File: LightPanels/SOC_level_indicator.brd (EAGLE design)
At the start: 161.2 x 162.3 mm, 163 parts, among them IC1 LM1084-ADJ

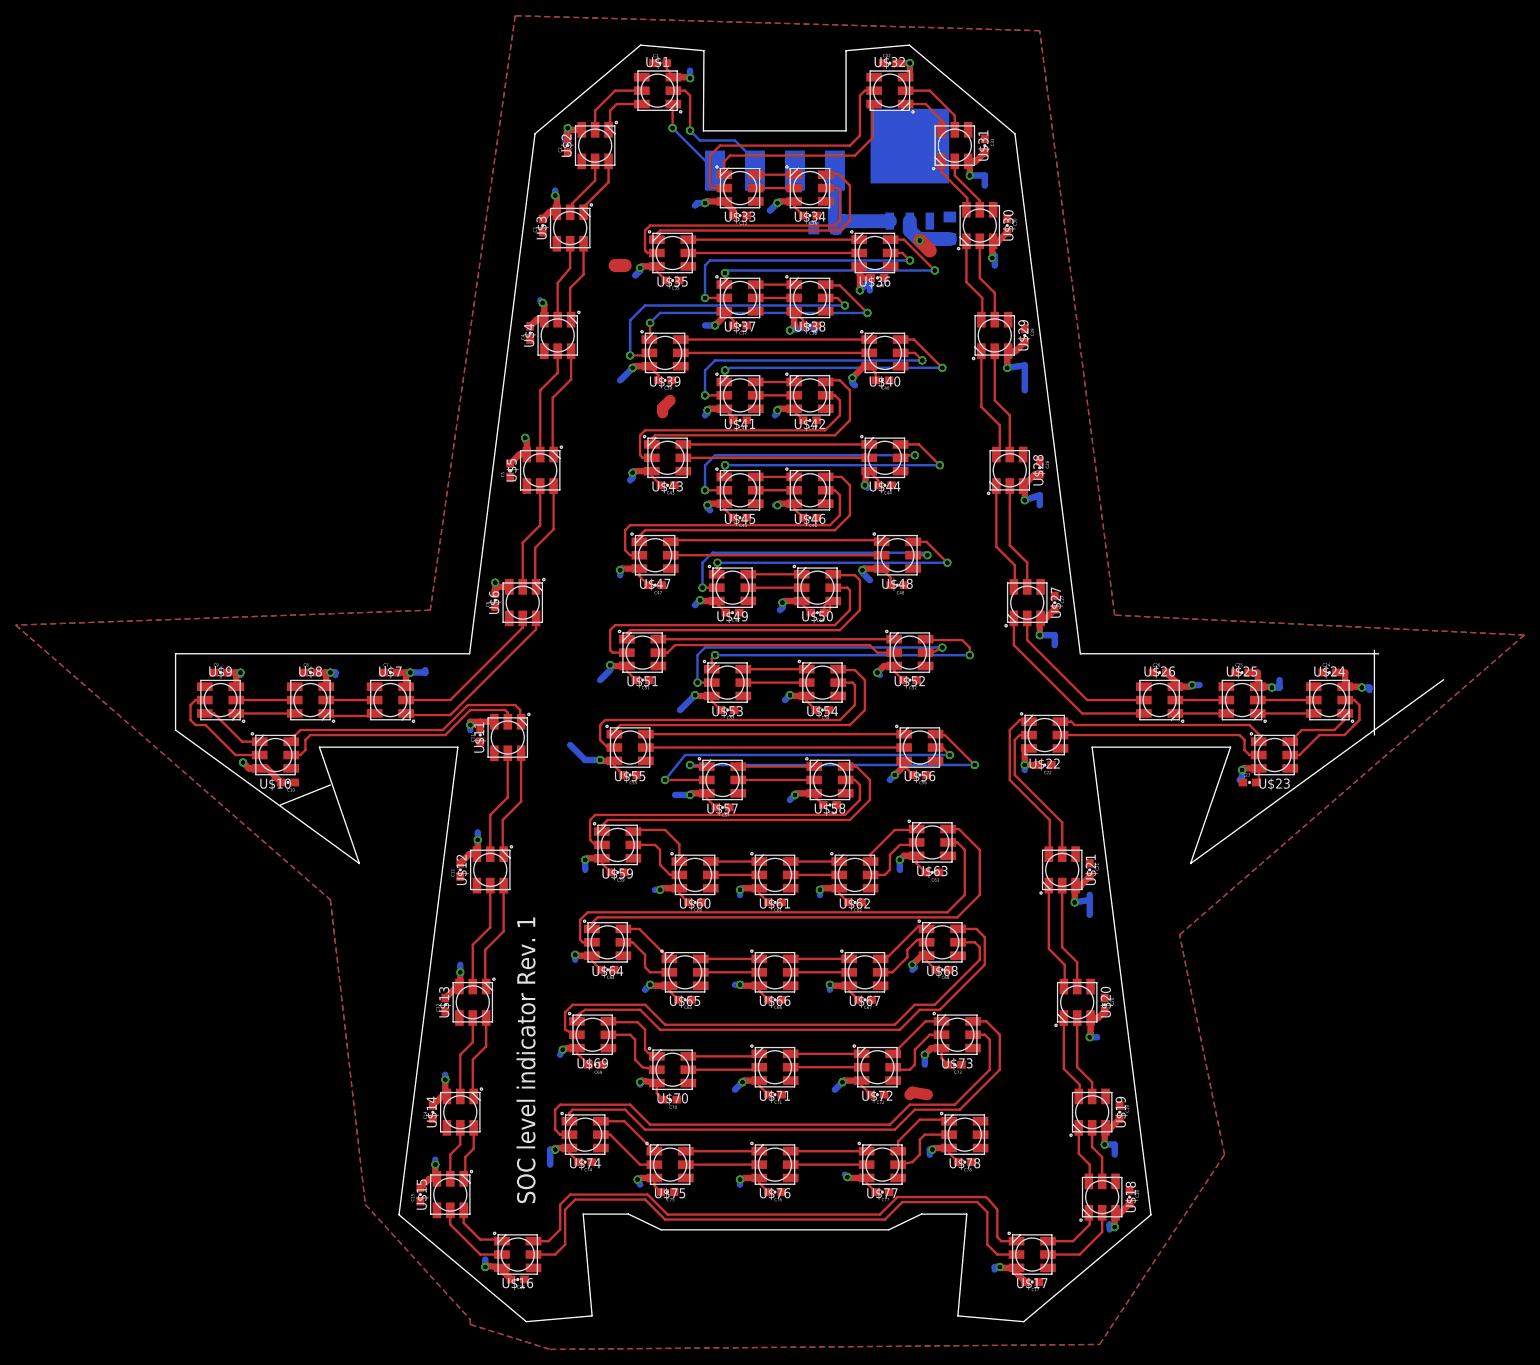
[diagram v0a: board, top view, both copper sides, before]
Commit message: Clean up light panels. Remvoe names/values
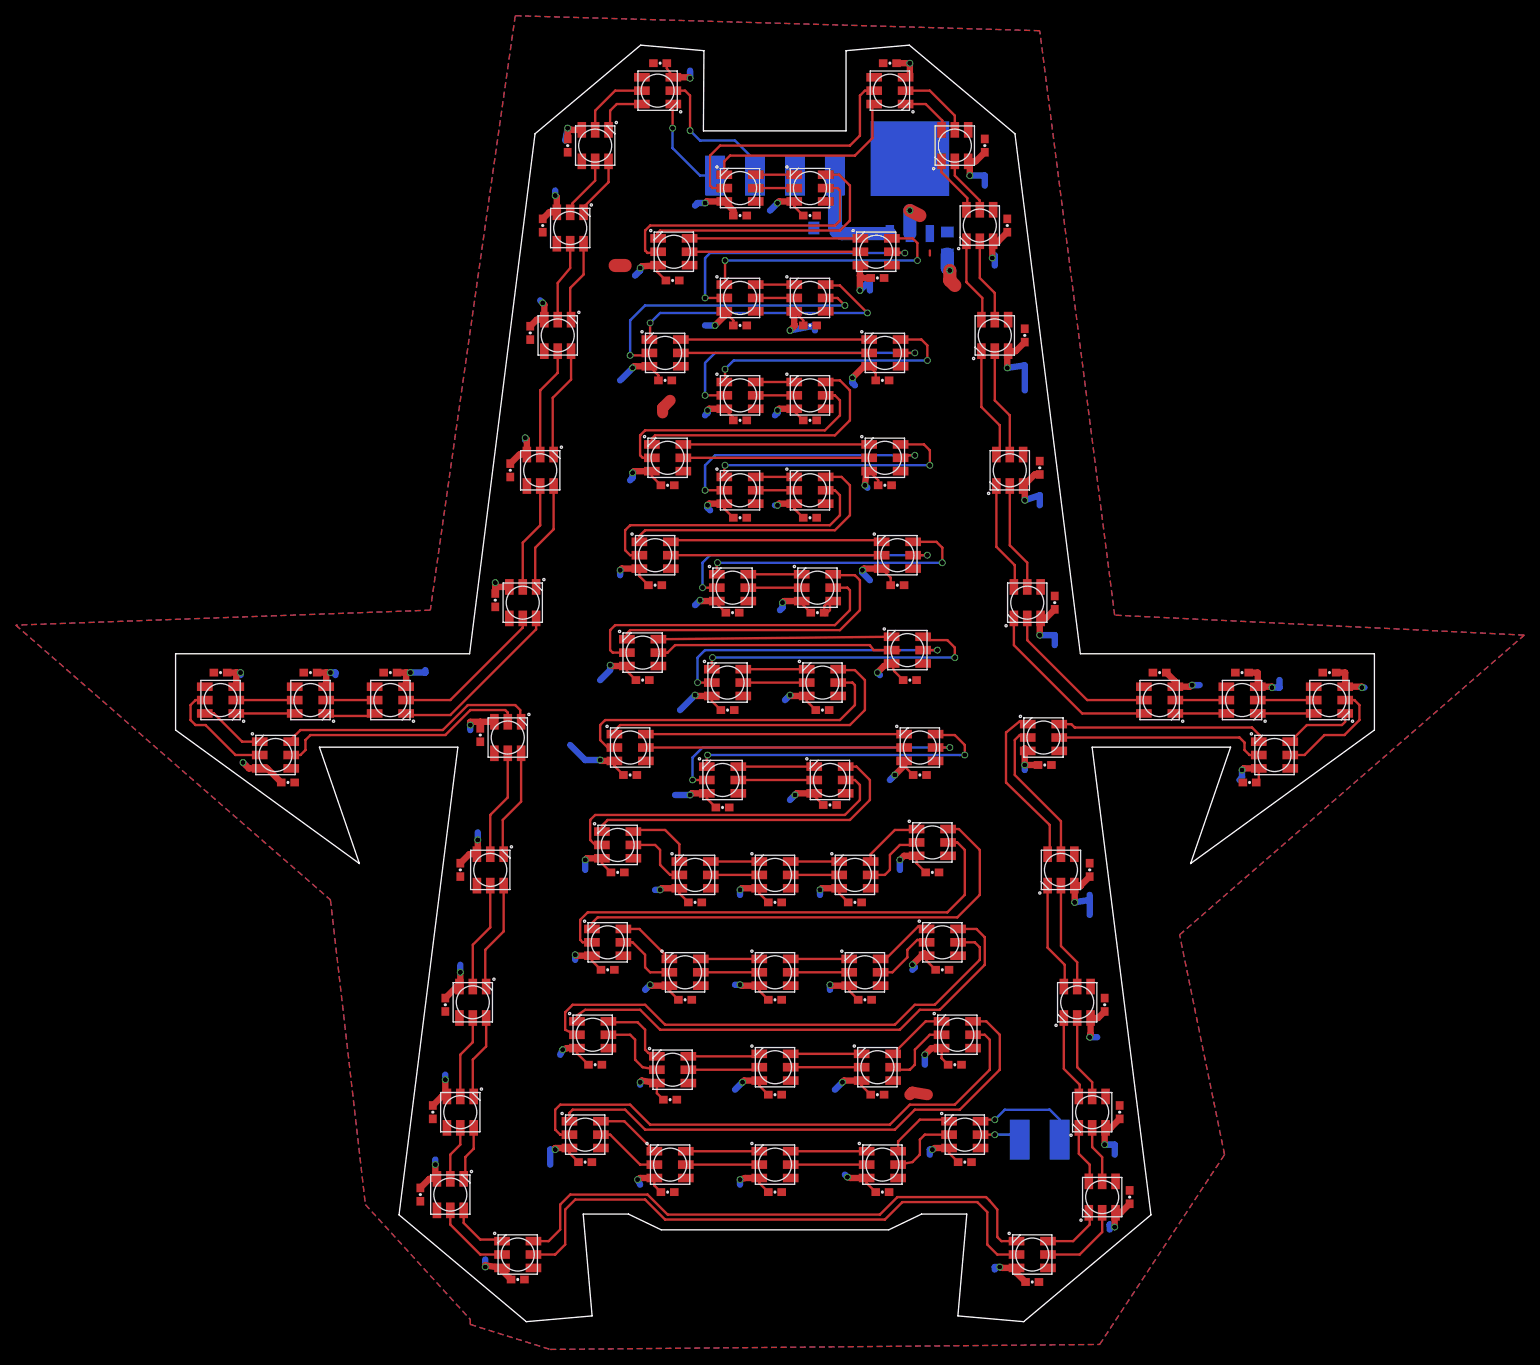
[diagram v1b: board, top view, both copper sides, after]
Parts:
- removed PAD1, PAD2, PAD3, PAD4: WIREPADSMD5-2,5, wirepad:5-2,5
- added +12V, CI, CO, DI, DO, GND: WIREPADSMD5-2,5, wirepad:5-2,5
- moved C79 1.93 mm to (94.3, 142.6)
- moved IC1 1.59 mm to (89.5, 149.5)
- moved U$52 0.45 mm to (89.2, 90.8)
- moved U$22 0.35 mm to (106.5, 79.7)
- moved U$35 0.22 mm to (59.5, 141.4)
- moved U$36 0.22 mm to (85.2, 141.4)
- moved U$21 0.16 mm to (108.7, 62.9)
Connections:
- net +12V: now also +12V.1; no longer PAD3.1
- net GND: now also GND.1; no longer PAD4.1
- net N$149: now also DI.1; no longer PAD1.1
- net N$150: now also CI.1; no longer PAD2.1
- net N$151: now also DO.1
- net N$152: now also CO.1
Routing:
- net N$151: track 0.00 -> 13.7 mm, vias 0 -> 1
- net N$123: track 45.2 -> 39.7 mm
- net N$124: track 45.0 -> 39.8 mm
- net N$152: track 0.00 -> 5.13 mm, vias 0 -> 1
- net N$108: track 41.4 -> 38.2 mm
- net N$92: track 36.0 -> 33.5 mm
- net N$76: track 35.6 -> 33.3 mm
- net N$149: track 10.7 -> 12.5 mm
- net N$90: track 34.9 -> 33.5 mm
- net N$107: track 39.1 -> 37.7 mm
- net N$91: track 37.4 -> 36.0 mm
- net N$75: track 35.7 -> 34.8 mm
- net +5V: track 19.1 -> 19.9 mm, vias 1 -> 2
- net N$150: track 17.9 -> 18.6 mm
- net N$37: track 21.0 -> 21.6 mm
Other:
- board size 161.2 x 162.3 mm -> 152.4 x 162.3 mm
- board text added: "SOC Level Indicator Rev. 1"
- board text removed: "SOC level indicator Rev. 1"
